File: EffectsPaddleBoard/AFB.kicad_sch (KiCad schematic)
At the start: 25 parts, among them J5 AudioJack2, J6 AudioJack2, U5 MCP6401T-xLT, U6 MCP6401T-xLT, U7 MCP6401T-xLT

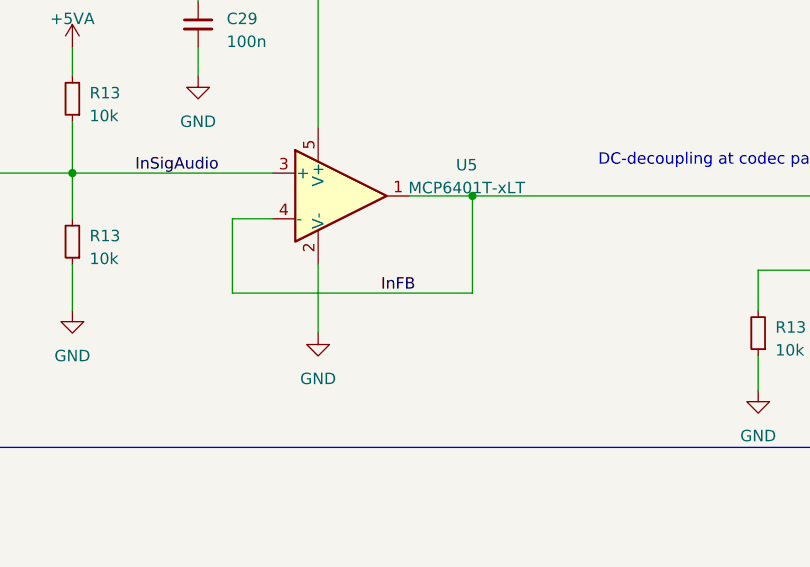
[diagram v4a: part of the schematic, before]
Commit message: Added 3d models
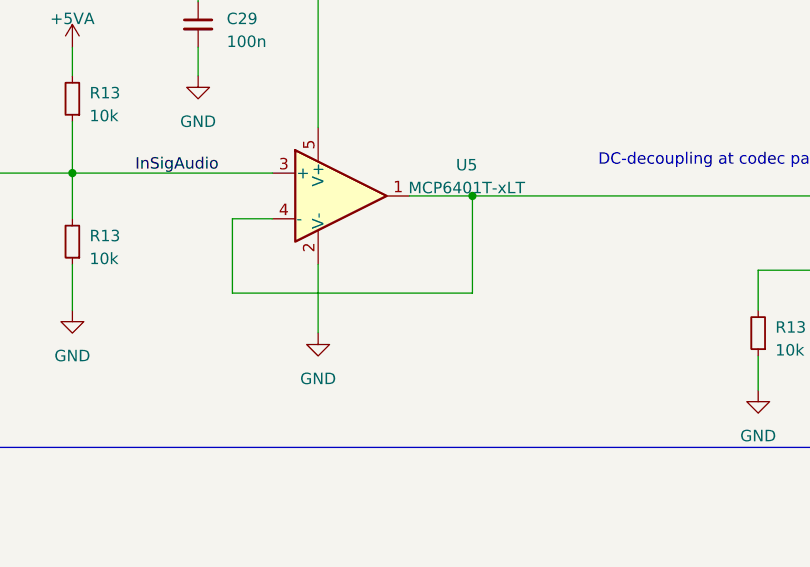
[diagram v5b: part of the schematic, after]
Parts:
- J5, J6: Distributer Link (none) -> https://www.mouser.ch/ProductDetail/Neutrik/NJ3FD-V?qs=JfNP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; Manufacturer (none) -> Neutrik; Manufacturer Part Number (none) -> NJ3FD-V

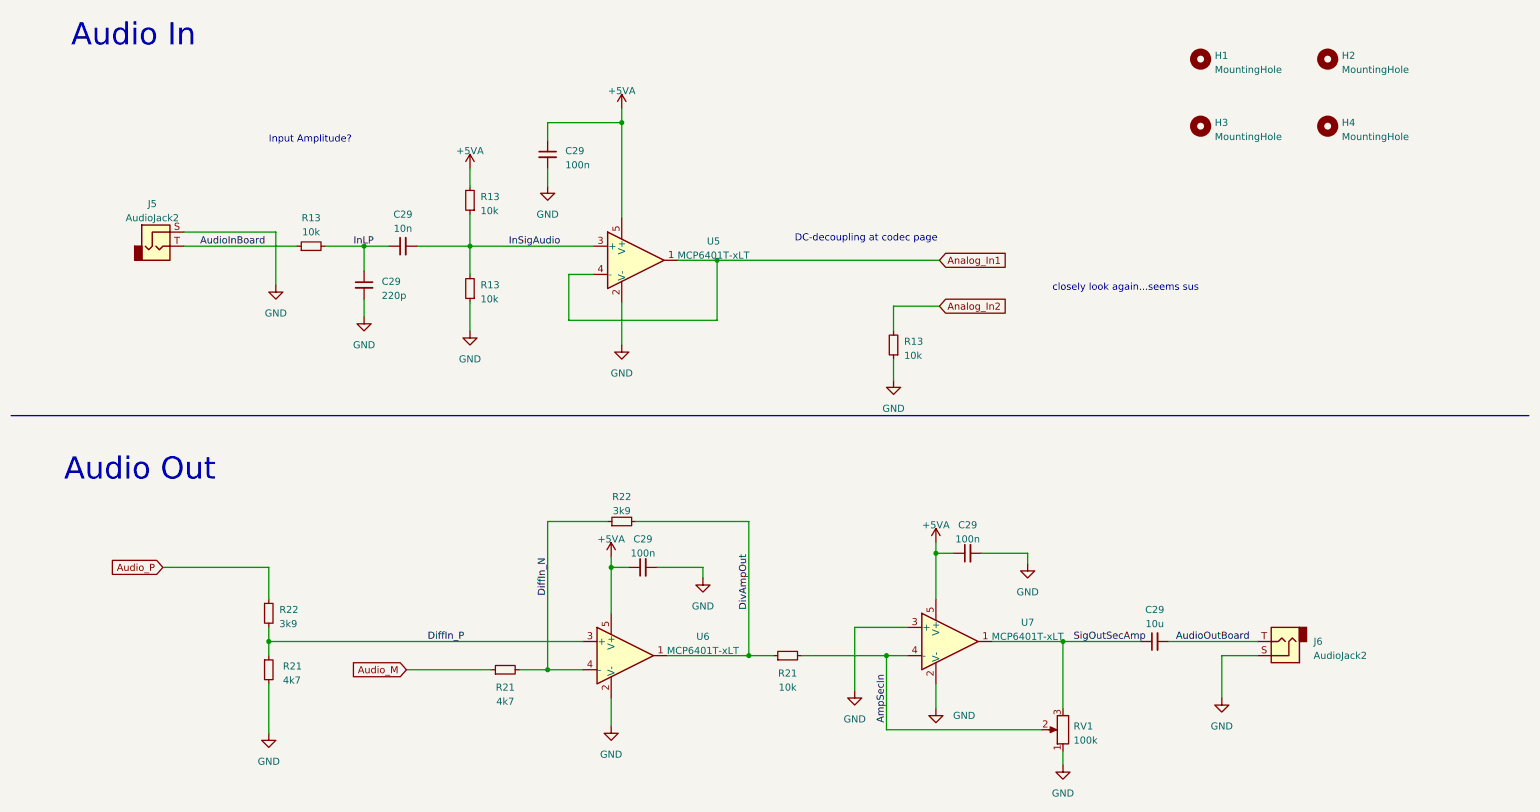
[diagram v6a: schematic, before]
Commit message: Tried separating analog and digital part
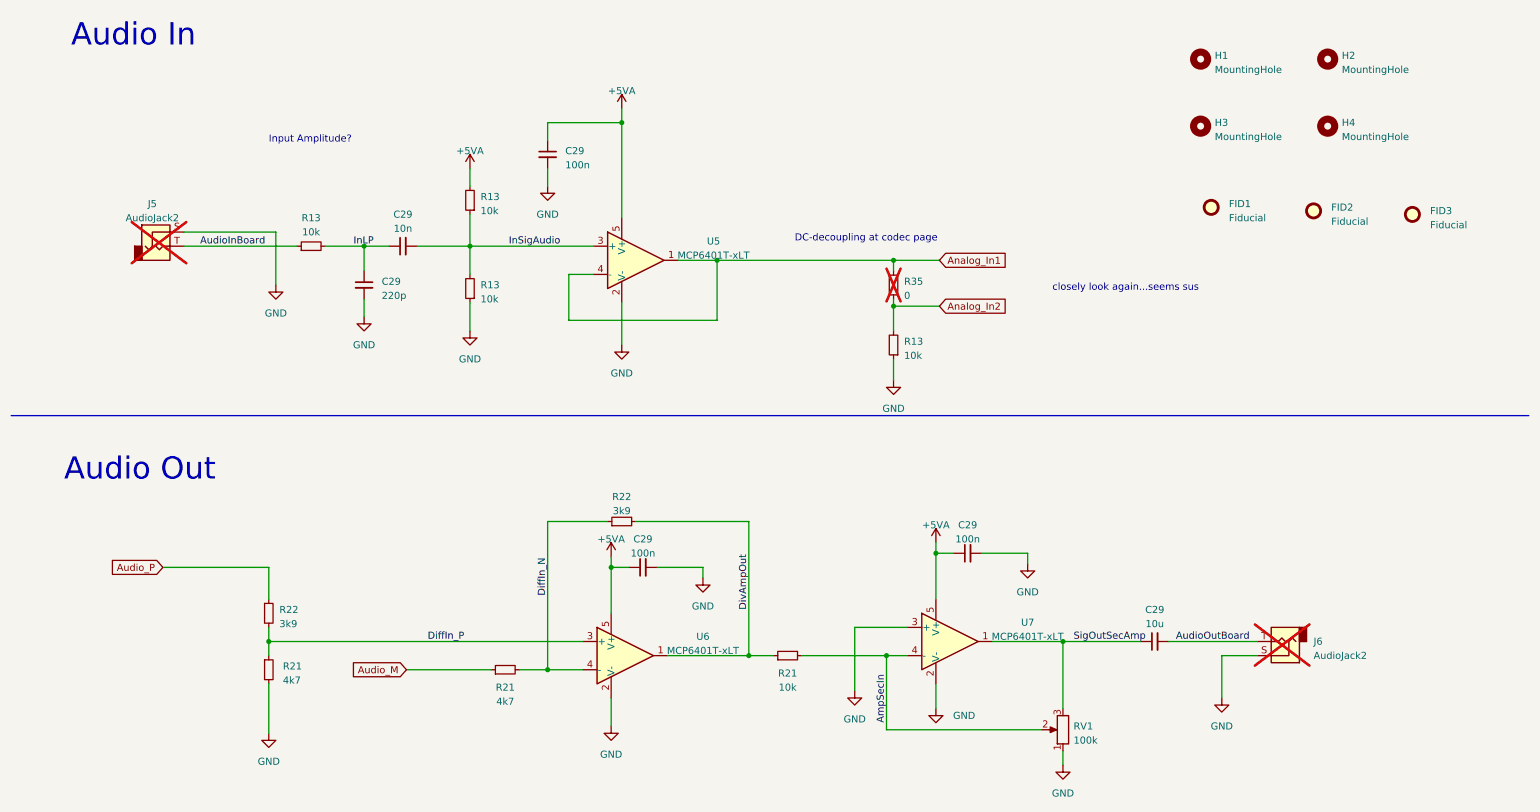
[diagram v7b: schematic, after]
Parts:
- added FID1, FID2, FID3: Fiducial, Fiducial:Fiducial_1mm_Mask2mm, symbol Mechanical:Fiducial
- added R35: 0, Resistor_SMD:R_0402_1005Metric, symbol Device:R_Small
- C29: Distributer Link (none) -> https://www.mouser.ch/ProductDetail/Murata-Electronics/GRM1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; Manufacturer (none) -> Murata Electronics; Manufacturer Part Number (none) -> GRM152R61A104KE19D
- C29: Distributer Link (none) -> https://www.mouser.ch/ProductDetail/Murata-Electronics/GRM3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; Manufacturer (none) -> Murata Electronics; Manufacturer Part Number (none) -> GRM31CR71C106KAC7L
- H1, H2, H3, H4: now left out of the parts list
- J5, J6: now not fitted; now left out of the parts list
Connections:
- net Analog_In1: now also R35.1
- net Analog_In2: now also R35.2
